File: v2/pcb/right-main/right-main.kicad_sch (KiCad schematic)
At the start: 33 parts, among them J1 Conn_01x10, SW1 SW_Push, SW10 SW_Push, SW11 SW_Push, SW12 SW_Push, SW13 SW_Push, SW14 SW_Push, SW15 SW_Push, SW16 SW_Push, SW2 SW_Push, SW3 SW_Push, SW4 SW_Push, SW5 SW_Push, SW6 SW_Push, SW7 SW_Push, SW8 SW_Push, SW9 SW_Push

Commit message: feat: update case data
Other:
- title: kobu2 left-main -> kobu2 right-main
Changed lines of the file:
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@@
 	(paper "A4")
 	(title_block
-		(title "kobu2 left-main")
+		(title "kobu2 right-main")
 		(date "2026-07-07")
 		(rev "v2")
@@
 		)
 		(instances
-			(project "left-main"
+			(project "right-main"
 				(path "/4b8088fe-122a-4bba-8ade-3fc2ea99e583"
 					(reference "#PWR02")
@@
 		)
 		(instances
-			(project "left-main"
+			(project "right-main"
 				(path "/4b8088fe-122a-4bba-8ade-3fc2ea99e583"
 					(reference "SW11")
@@
 		)
 		(instances
-			(project "left-main"
+			(project "right-main"
 				(path "/4b8088fe-122a-4bba-8ade-3fc2ea99e583"
 					(reference "D11")
@@
 		)
 		(instances
-			(project "left-main"
+			(project "right-main"
 				(path "/4b8088fe-122a-4bba-8ade-3fc2ea99e583"
 					(reference "SW8")
@@
 		)
 		(instances
-			(project "left-main"
+			(project "right-main"
 				(path "/4b8088fe-122a-4bba-8ade-3fc2ea99e583"
 					(reference "SW2")
@@
 		)
 		(instances
-			(project "left-main"
+			(project "right-main"
 				(path "/4b8088fe-122a-4bba-8ade-3fc2ea99e583"
 					(reference "D9")
@@
 		)
 		(instances
-			(project "left-main"
+			(project "right-main"
 				(path "/4b8088fe-122a-4bba-8ade-3fc2ea99e583"
 					(reference "J1")
@@
 		)
 		(instances
-			(project "left-main"
+			(project "right-main"
 				(path "/4b8088fe-122a-4bba-8ade-3fc2ea99e583"
 					(reference "D7")
@@
 		)
 		(instances
-			(project "left-main"
+			(project "right-main"
 				(path "/4b8088fe-122a-4bba-8ade-3fc2ea99e583"
 					(reference "SW12")
@@
 		)
 		(instances
-			(project "left-main"
+			(project "right-main"
 				(path "/4b8088fe-122a-4bba-8ade-3fc2ea99e583"
 					(reference "SW1")
@@
 		)
 		(instances
-			(project "left-main"
+			(project "right-main"
 				(path "/4b8088fe-122a-4bba-8ade-3fc2ea99e583"
 					(reference "D3")
@@
 		)
 		(instances
-			(project "left-main"
+			(project "right-main"
 				(path "/4b8088fe-122a-4bba-8ade-3fc2ea99e583"
 					(reference "#FLG02")
@@
 		)
 		(instances
-			(project "left-main"
+			(project "right-main"
 				(path "/4b8088fe-122a-4bba-8ade-3fc2ea99e583"
 					(reference "SW9")
@@
 		)
 		(instances
-			(project "left-main"
+			(project "right-main"
 				(path "/4b8088fe-122a-4bba-8ade-3fc2ea99e583"
 					(reference "D4")
@@
 		)
 		(instances
-			(project "left-main"
+			(project "right-main"
 				(path "/4b8088fe-122a-4bba-8ade-3fc2ea99e583"
 					(reference "D6")
@@
 		)
 		(instances
-			(project "left-main"
+			(project "right-main"
 				(path "/4b8088fe-122a-4bba-8ade-3fc2ea99e583"
 					(reference "D13")
@@
 		)
 		(instances
-			(project "left-main"
+			(project "right-main"
 				(path "/4b8088fe-122a-4bba-8ade-3fc2ea99e583"
 					(reference "SW6")
@@
 		)
 		(instances
-			(project "left-main"
+			(project "right-main"
 				(path "/4b8088fe-122a-4bba-8ade-3fc2ea99e583"
 					(reference "SW3")
@@
 		)
 		(instances
-			(project "left-main"
+			(project "right-main"
 				(path "/4b8088fe-122a-4bba-8ade-3fc2ea99e583"
 					(reference "D2")
@@
 		)
 		(instances
-			(project "left-main"
+			(project "right-main"
 				(path "/4b8088fe-122a-4bba-8ade-3fc2ea99e583"
 					(reference "D8")
@@
 		)
 		(instances
-			(project "left-main"
+			(project "right-main"
 				(path "/4b8088fe-122a-4bba-8ade-3fc2ea99e583"
 					(reference "SW5")
@@
 		)
 		(instances
-			(project "left-main"
+			(project "right-main"
 				(path "/4b8088fe-122a-4bba-8ade-3fc2ea99e583"
 					(reference "D1")
@@
 		)
 		(instances
-			(project "left-main"
+			(project "right-main"
 				(path "/4b8088fe-122a-4bba-8ade-3fc2ea99e583"
 					(reference "SW7")
@@
 		)
 		(instances
-			(project "left-main"
+			(project "right-main"
 				(path "/4b8088fe-122a-4bba-8ade-3fc2ea99e583"
 					(reference "D12")
@@
 		)
 		(instances
-			(project "left-main"
+			(project "right-main"
 				(path "/4b8088fe-122a-4bba-8ade-3fc2ea99e583"
 					(reference "D10")
@@
 		)
 		(instances
-			(project "left-main"
+			(project "right-main"
 				(path "/4b8088fe-122a-4bba-8ade-3fc2ea99e583"
 					(reference "D15")
@@
 		)
 		(instances
-			(project "left-main"
+			(project "right-main"
 				(path "/4b8088fe-122a-4bba-8ade-3fc2ea99e583"
 					(reference "SW13")
@@
 		)
 		(instances
-			(project "left-main"
+			(project "right-main"
 				(path "/4b8088fe-122a-4bba-8ade-3fc2ea99e583"
 					(reference "D5")
@@
 		)
 		(instances
-			(project "left-main"
+			(project "right-main"
 				(path "/4b8088fe-122a-4bba-8ade-3fc2ea99e583"
 					(reference "SW10")
@@
 		)
 		(instances
-			(project "left-main"
+			(project "right-main"
 				(path "/4b8088fe-122a-4bba-8ade-3fc2ea99e583"
 					(reference "SW15")
@@
 		)
 		(instances
-			(project "left-main"
+			(project "right-main"
 				(path "/4b8088fe-122a-4bba-8ade-3fc2ea99e583"
 					(reference "SW14")
@@
 		)
 		(instances
-			(project "left-main"
+			(project "right-main"
 				(path "/4b8088fe-122a-4bba-8ade-3fc2ea99e583"
 					(reference "SW4")
@@
 		)
 		(instances
-			(project "left-main"
+			(project "right-main"
 				(path "/4b8088fe-122a-4bba-8ade-3fc2ea99e583"
 					(reference "D14")
@@
 		)
 		(instances
-			(project "left-main"
+			(project "right-main"
 				(path "/4b8088fe-122a-4bba-8ade-3fc2ea99e583"
 					(reference "SW16")
@@
 		)
 		(instances
-			(project "left-main"
+			(project "right-main"
 				(path "/4b8088fe-122a-4bba-8ade-3fc2ea99e583"
 					(reference "D16")

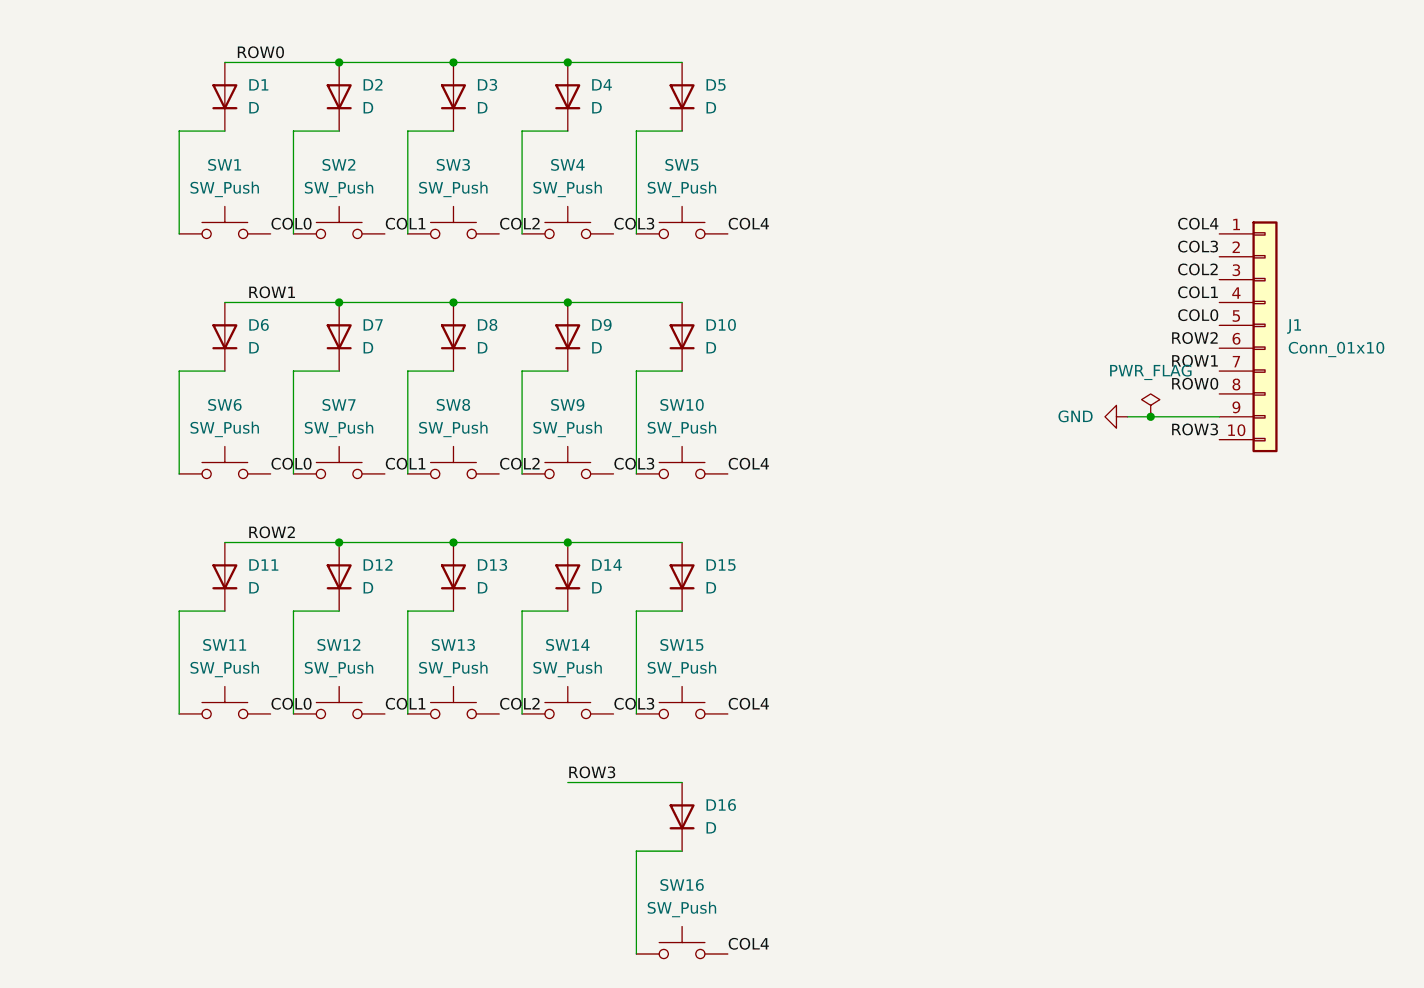
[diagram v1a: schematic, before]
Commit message: feat: add right main pcb
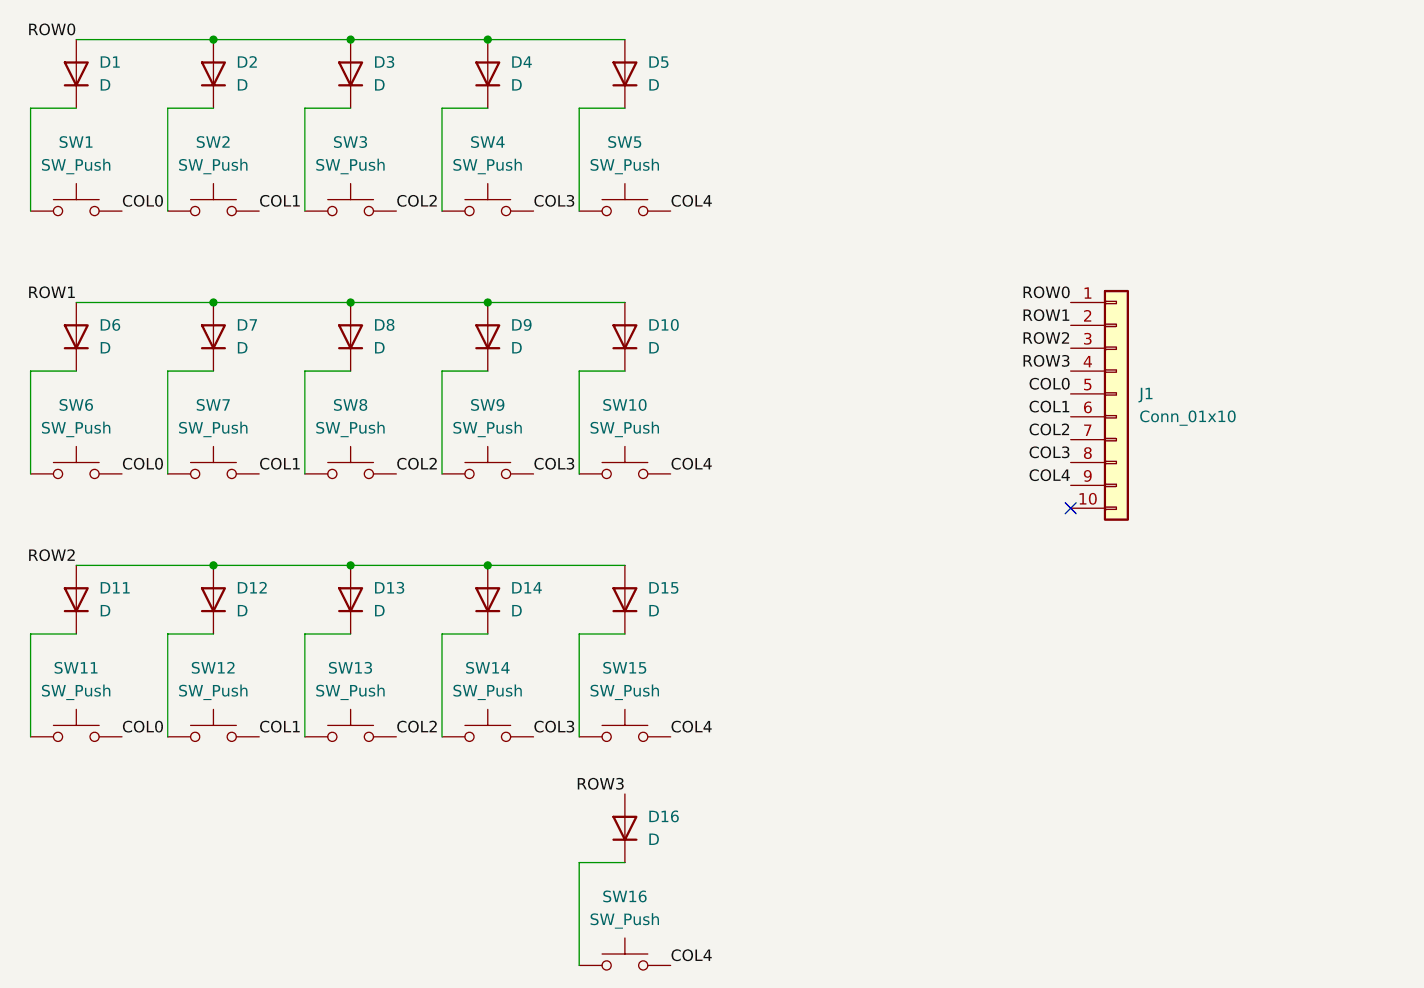
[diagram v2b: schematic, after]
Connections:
- net GND is gone; now on net COL4: J1.9 (Pin_9)
- net COL1: now also J1.6 (Pin_6); no longer J1.4 (Pin_4)
- net COL2: now also J1.7 (Pin_7); no longer J1.3 (Pin_3)
- net COL3: now also J1.8 (Pin_8); no longer J1.2 (Pin_2)
- net COL4: no longer J1.1 (Pin_1)
- net ROW0: now also J1.1 (Pin_1); no longer J1.8 (Pin_8)
- net ROW1: now also J1.2 (Pin_2); no longer J1.7 (Pin_7)
- net ROW2: now also J1.3 (Pin_3); no longer J1.6 (Pin_6)
- net ROW3: now also J1.4 (Pin_4); no longer J1.10 (Pin_10)
- no-connect marks 0 -> 1
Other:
- title: kobu2 right-main -> (none)
